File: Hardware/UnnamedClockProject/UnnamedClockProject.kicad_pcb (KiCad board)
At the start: 2 copper layers, 160 x 102 mm, 38 parts, among them J101 CLOCK_OUT, J102 POWER, J103 BUTTONS, Q101 2N3904, U104 G3MB-202P, U105 G3MB-202P, U106 G3MB-202P, U107 CAT24C256

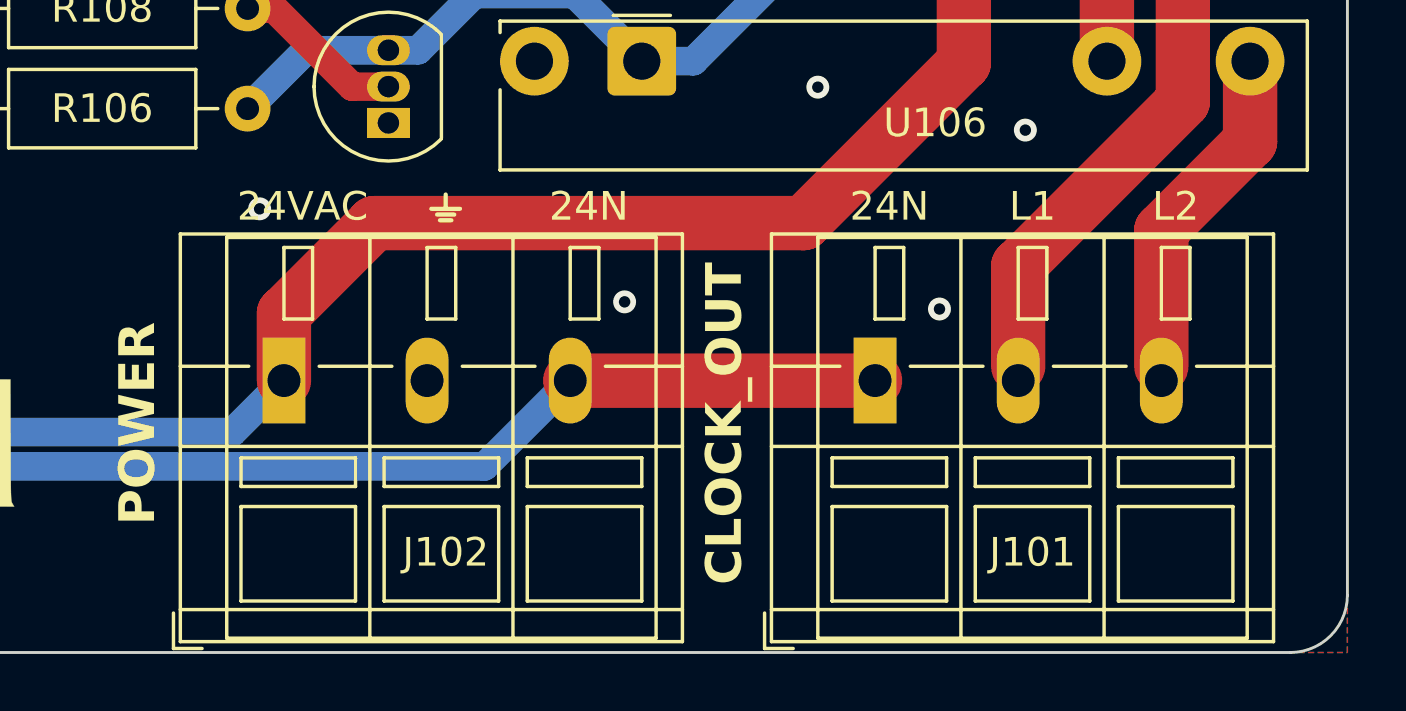
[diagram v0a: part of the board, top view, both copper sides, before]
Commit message: Add 3d models
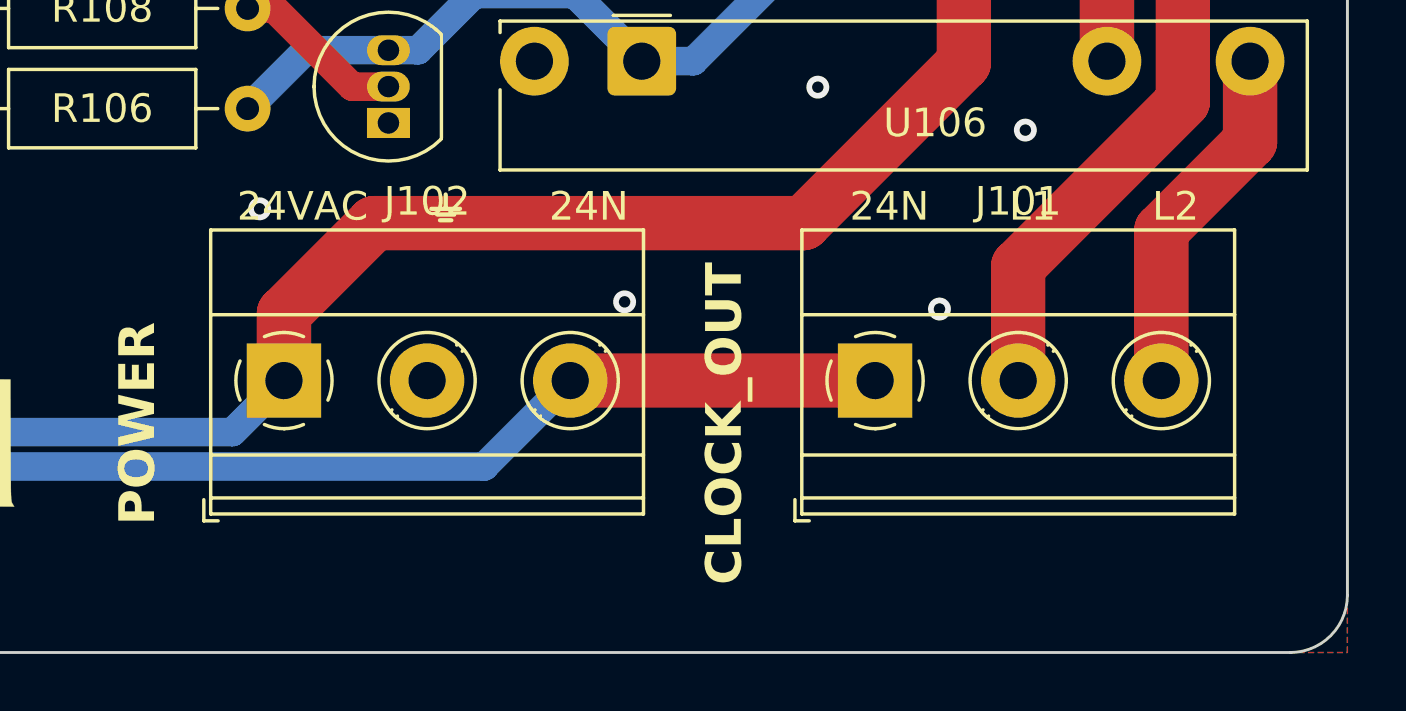
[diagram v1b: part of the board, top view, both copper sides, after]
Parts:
- J101, J102: footprint TerminalBlock_WAGO:TerminalBlock_WAGO_236-103_1x03_P5.00mm_45Degree -> TerminalBlock_Phoenix:TerminalBlock_Phoenix_MKDS-1,5-3_1x03_P5.00mm_Horizontal

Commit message: Boilerplate new file upstream
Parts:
- U104, U105, U106: footprint OptoDevice:Finder_34.81 -> ac1ja:OptoRelay
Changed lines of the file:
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@@
     )
   )
-  (footprint "OptoDevice:Finder_34.81" (layer "F.Cu")
+  (footprint "ac1ja:OptoRelay" (layer "F.Cu")
     (at 43.35 33.3425)
     (descr "Relay SPST, Finder Type 34.81 (opto relays/coupler), vertical/standing form, see https://gfinder.findernet.com/public/attachments/34/EN/S34USAEN.pdf")
@@
     (property "ki_keywords" "Photo-Triac Opto Triac")
     (attr through_hole)
-    (fp_text reference "U105" (at 10.25 2.1575) (layer "F.SilkS")
+    (fp_text reference "U105" (at 10.25 -2.2) (layer "F.SilkS")
         (effects (font (size 1 1) (thickness 0.15)))
     )
@@
     )
   )
-  (footprint "OptoDevice:Finder_34.81" (layer "F.Cu")
+  (footprint "ac1ja:OptoRelay" (layer "F.Cu")
     (at 43.35 39.3425)
     (descr "Relay SPST, Finder Type 34.81 (opto relays/coupler), vertical/standing form, see https://gfinder.findernet.com/public/attachments/34/EN/S34USAEN.pdf")
@@
     (property "ki_keywords" "Photo-Triac Opto Triac")
     (attr through_hole)
-    (fp_text reference "U106" (at 10.25 2.1575) (layer "F.SilkS")
+    (fp_text reference "U106" (at 10.25 -2.2) (layer "F.SilkS")
         (effects (font (size 1 1) (thickness 0.15)))
     )
@@
     )
   )
-  (footprint "OptoDevice:Finder_34.81" (layer "F.Cu")
+  (footprint "ac1ja:OptoRelay" (layer "F.Cu")
     (at 38.35 27.3425)
     (descr "Relay SPST, Finder Type 34.81 (opto relays/coupler), vertical/standing form, see https://gfinder.findernet.com/public/attachments/34/EN/S34USAEN.pdf")
@@
     (property "ki_keywords" "Photo-Triac Opto Triac")
     (attr through_hole)
-    (fp_text reference "U104" (at 10.25 2.1575) (layer "F.SilkS")
-        (effects (font (size 1 1) (thickness 0.15)))
-    )
+    (fp_text reference "U104" (at 10.25 -2.2) (layer "F.SilkS")
+        (effects (font (size 1 1) (thickness 0.15)))
+    )
